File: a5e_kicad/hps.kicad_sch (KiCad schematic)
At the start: 17 parts, among them J8 Micro_SD_Card, U11 NXS0506GUX, U40 TPS2116DRLR, U41 TPS22918DBVR, U7 A5EB013B-B23B

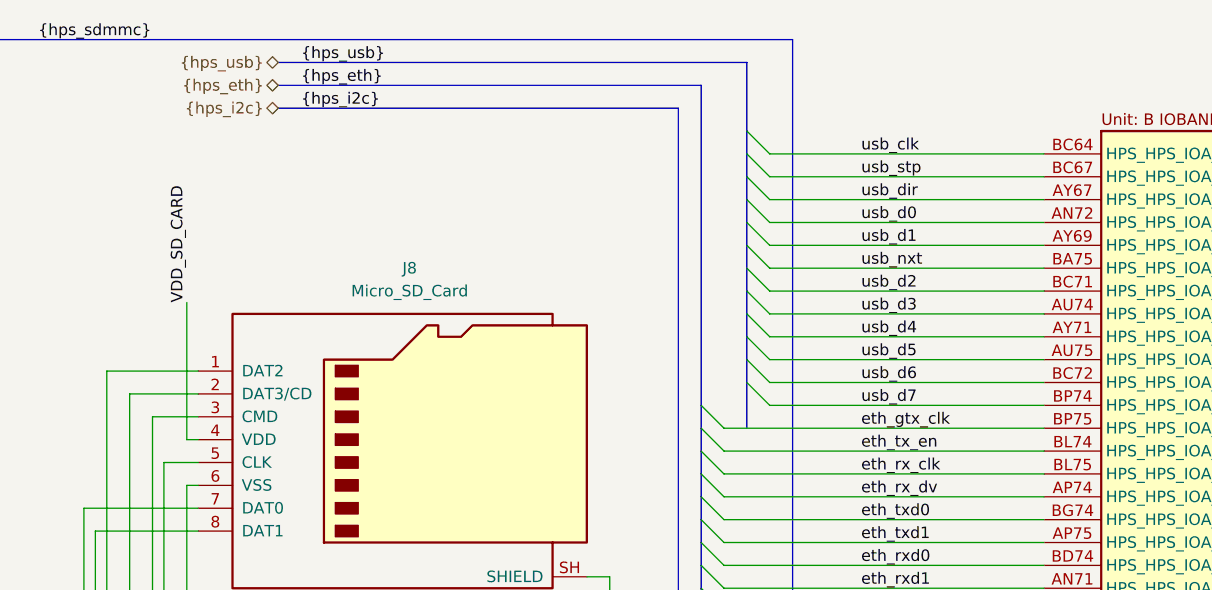
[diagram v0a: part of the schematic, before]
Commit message: Remove unused USB leftovers
USB is not used on this board.
- HPS sheet: remove the {hps_usb} ULPI bus, labels and wires; the 12
  U7 USB0 pins get no-connect flags
- Connectors sheet: remove the {usb_phy} hierarchical label and bus
- Clock sheet: remove the unused clk4 (USB 24 MHz) outputs and note
- Top-level: remove the {hps_usb}, {usb_phy}, clk4_P/clk4_N sheet pins
  and the usb_clk24 net

Netlist compared before/after: only the 12 USB pin nets changed (now
unconnected). ERC 542 -> 522.
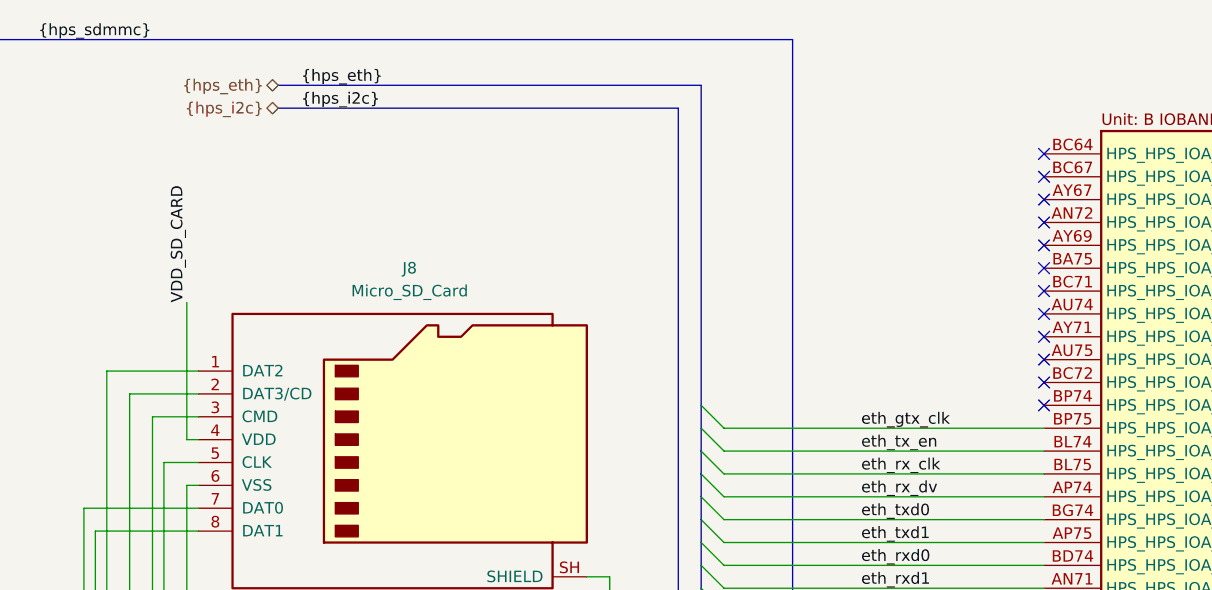
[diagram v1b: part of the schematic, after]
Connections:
- net usb_clk: no longer names the net of U7.BC64 (HPS_HPS_IOA_1_GPIO0_IO0)
- net usb_d0: no longer names the net of U7.AN72 (HPS_HPS_IOA_4_GPIO0_IO3)
- net usb_d1: no longer names the net of U7.AY69 (HPS_HPS_IOA_5_GPIO0_IO4)
- net usb_d2: no longer names the net of U7.BC71 (HPS_HPS_IOA_7_GPIO0_IO6)
- net usb_d3: no longer names the net of U7.AU74 (HPS_HPS_IOA_8_GPIO0_IO7)
- net usb_d4: no longer names the net of U7.AY71 (HPS_HPS_IOA_9_GPIO0_IO8)
- net usb_d5: no longer names the net of U7.AU75 (HPS_HPS_IOA_10_GPIO0_IO9)
- net usb_d6: no longer names the net of U7.BC72 (HPS_HPS_IOA_11_GPIO0_IO10)
- net usb_d7: no longer names the net of U7.BP74 (HPS_HPS_IOA_12_GPIO0_IO11)
- net usb_dir: no longer names the net of U7.AY67 (HPS_HPS_IOA_3_GPIO0_IO2)
- net usb_nxt: no longer names the net of U7.BA75 (HPS_HPS_IOA_6_GPIO0_IO5)
- net usb_stp: no longer names the net of U7.BC67 (HPS_HPS_IOA_2_GPIO0_IO1)
- no-connect marks 5 -> 17
